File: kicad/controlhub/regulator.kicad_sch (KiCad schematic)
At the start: 16 parts, among them U1 LMR33630ARNXR

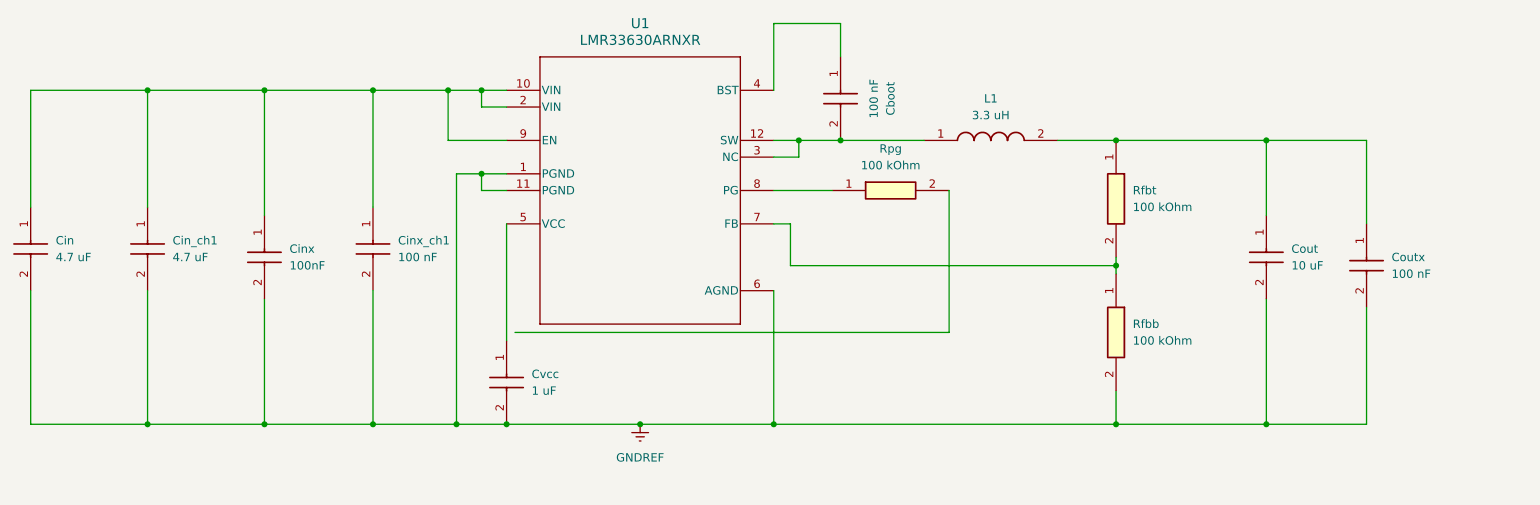
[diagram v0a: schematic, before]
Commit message: added converter and started servo driver
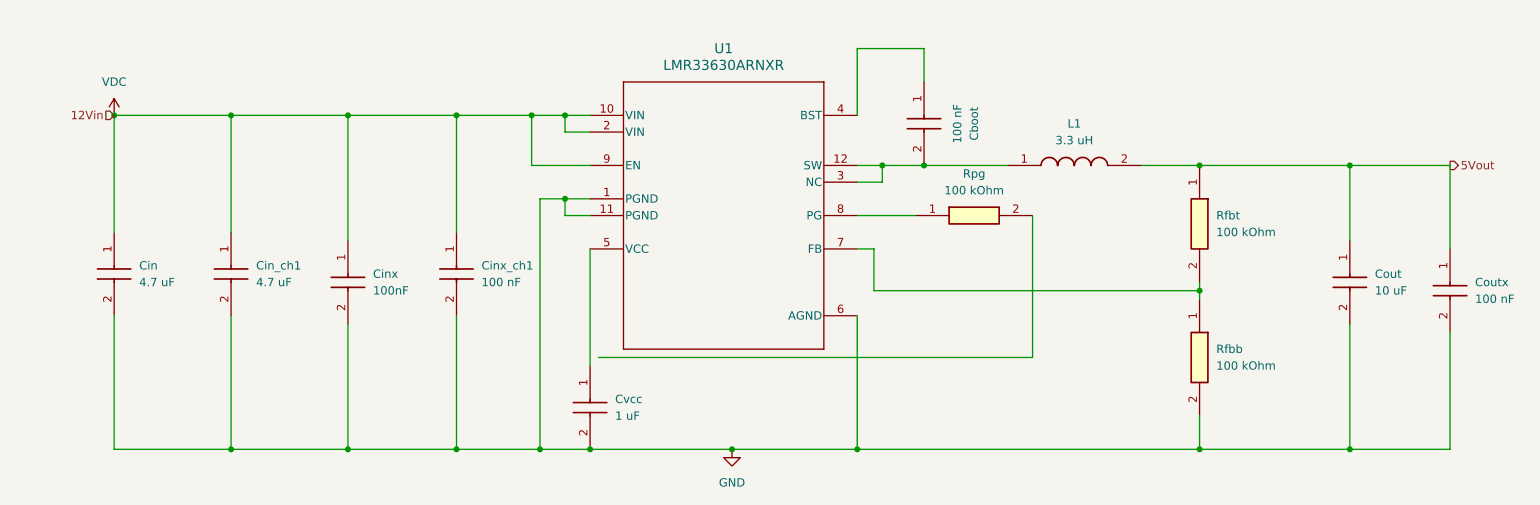
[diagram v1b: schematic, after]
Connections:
- net 5Vout: now reaches Cout.1, Coutx.1, L1.2, Rfbt.1
- net VDC: now reaches Cin.1, Cin_ch1.1, Cinx.1, Cinx_ch1.1, U1.10 (VIN), U1.2 (VIN), U1.9 (EN)
- net GNDREF renamed GND
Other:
- title: (none) -> Tensor Labs
- moved on the sheet: Cboot, Cin, Cin_ch1, Cinx, Cinx_ch1, Cout, Coutx, Cvcc, L1, Rfbb, Rfbt, Rpg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
